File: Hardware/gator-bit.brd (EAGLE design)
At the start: 114.4 x 70.4 mm, 95 parts, among them J1 GATOR, J10 GATOR, J11 GATOR, J12 GATOR, J13 GATOR, J14 GATOR, J15 GATOR, J16 GATOR, J17 GATOR, J18 GATOR, J2 GATOR, J3 GATOR, J4 GATOR, J6 GATOR, J7 GATOR, J8 GATOR, J9 GATOR, U1 TPS63070, U2 micro:bit, U3 TXB0104, U4 ADJ REG 1.5A

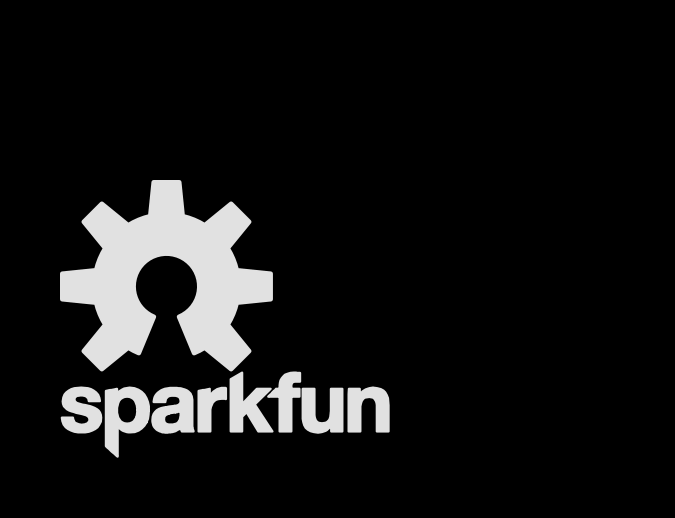
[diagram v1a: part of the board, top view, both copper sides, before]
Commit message: Updating per QC Review
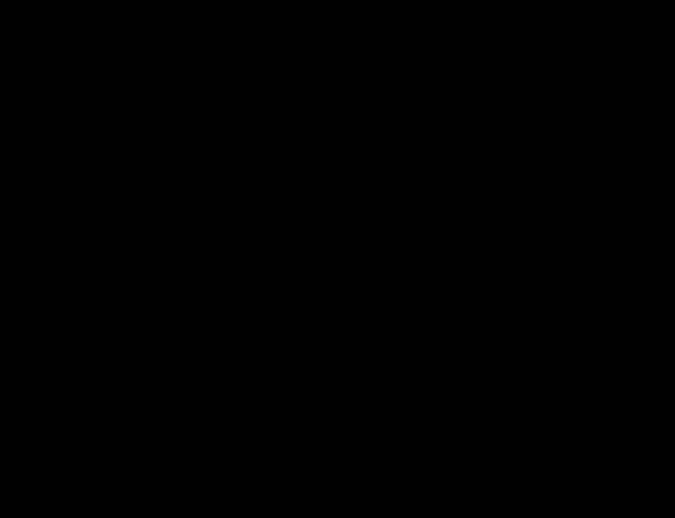
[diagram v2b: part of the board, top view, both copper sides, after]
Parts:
- removed LOGO1: OSHW-LOGOL, SparkFun-Aesthetics:OSHW-LOGO-L
- removed LOGO2: SFE_LOGO_NAME.1_INCH, SparkFun-Aesthetics:SFE_LOGO_NAME_.1
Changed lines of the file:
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@@
 <?xml version="1.0" encoding="utf-8"?>
 <!DOCTYPE eagle SYSTEM "eagle.dtd">
-<eagle version="7.7.0">
+<eagle version="8.5.1">
 <drawing>
 <settings>
 <setting alwaysvectorfont="no"/>
+<setting keepoldvectorfont="yes"/>
 <setting verticaltext="up"/>
 </settings>
@@
 <layers>
 <layer number="1" name="Top" color="4" fill="1" visible="yes" active="yes"/>
-<layer number="2" name="Route2" color="1" fill="3" visible="no" active="yes"/>
-<layer number="15" name="Route15" color="4" fill="6" visible="no" active="yes"/>
+<layer number="2" name="Route2" color="1" fill="3" visible="yes" active="yes"/>
+<layer number="15" name="Route15" color="4" fill="6" visible="yes" active="yes"/>
 <layer number="16" name="Bottom" color="1" fill="1" visible="yes" active="yes"/>
 <layer number="17" name="Pads" color="2" fill="1" visible="yes" active="yes"/>
@@
 <layer number="19" name="Unrouted" color="6" fill="1" visible="yes" active="yes"/>
 <layer number="20" name="Dimension" color="15" fill="1" visible="yes" active="yes"/>
-<layer number="21" name="tPlace" color="16" fill="1" visible="no" active="yes"/>
-<layer number="22" name="bPlace" color="14" fill="1" visible="no" active="yes"/>
+<layer number="21" name="tPlace" color="16" fill="1" visible="yes" active="yes"/>
+<layer number="22" name="bPlace" color="14" fill="1" visible="yes" active="yes"/>
 <layer number="23" name="tOrigins" color="15" fill="1" visible="yes" active="yes"/>
 <layer number="24" name="bOrigins" color="15" fill="1" visible="yes" active="yes"/>
-<layer number="25" name="tNames" color="7" fill="1" visible="no" active="yes"/>
-<layer number="26" name="bNames" color="7" fill="1" visible="no" active="yes"/>
-<layer number="27" name="tValues" color="7" fill="1" visible="no" active="yes"/>
-<layer number="28" name="bValues" color="7" fill="1" visible="no" active="yes"/>
+<layer number="25" name="tNames" color="7" fill="1" visible="yes" active="yes"/>
+<layer number="26" name="bNames" color="7" fill="1" visible="yes" active="yes"/>
+<layer number="27" name="tValues" color="7" fill="1" visible="yes" active="yes"/>
+<layer number="28" name="bValues" color="7" fill="1" visible="yes" active="yes"/>
 <layer number="29" name="tStop" color="7" fill="3" visible="yes" active="yes"/>
 <layer number="30" name="bStop" color="7" fill="6" visible="yes" active="yes"/>
@@
 <layer number="41" name="tRestrict" color="4" fill="10" visible="yes" active="yes"/>
 <layer number="42" name="bRestrict" color="1" fill="10" visible="yes" active="yes"/>
-<layer number="43" name="vRestrict" color="2" fill="10" visible="no" active="yes"/>
-<layer number="44" name="Drills" color="7" fill="1" visible="no" active="yes"/>
-<layer number="45" name="Holes" color="7" fill="1" visible="no" active="yes"/>
-<layer number="46" name="Milling" color="3" fill="1" visible="no" active="yes"/>
-<layer number="47" name="Measures" color="7" fill="1" visible="no" active="yes"/>
-<layer number="51" name="tDocu" color="6" fill="1" visible="no" active="yes"/>
-<layer number="52" name="bDocu" color="7" fill="1" visible="no" active="yes"/>
+<layer number="43" name="vRestrict" color="2" fill="10" visible="yes" active="yes"/>
+<layer number="44" name="Drills" color="7" fill="1" visible="yes" active="yes"/>
+<layer number="45" name="Holes" color="7" fill="1" visible="yes" active="yes"/>
+<layer number="46" name="Milling" color="3" fill="1" visible="yes" active="yes"/>
+<layer number="47" name="Measures" color="7" fill="1" visible="yes" active="yes"/>
+<layer number="51" name="tDocu" color="6" fill="1" visible="yes" active="yes"/>
+<layer number="52" name="bDocu" color="7" fill="1" visible="yes" active="yes"/>
 <layer number="3" name="Route3" color="4" fill="3" visible="no" active="no"/>
 <layer number="4" name="Route4" color="1" fill="4" visible="no" active="no"/>
@@
 <layer number="230" name="230bmp" color="7" fill="1" visible="no" active="no"/>
 <layer number="231" name="231bmp" color="7" fill="1" visible="no" active="no"/>
-<layer number="232" name="Eagle3D_PG2" color="7" fill="1" visible="no" active="yes"/>
-<layer number="233" name="Eagle3D_PG3" color="7" fill="1" visible="no" active="yes"/>
+<layer number="232" name="Eagle3D_PG2" color="7" fill="1" visible="yes" active="yes"/>
+<layer number="233" name="Eagle3D_PG3" color="7" fill="1" visible="yes" active="yes"/>
 <layer number="248" name="Housing" color="7" fill="1" visible="no" active="no"/>
 <layer number="249" name="Edge" color="7" fill="1" visible="no" active="no"/>
@@
 <param name="dpMaxLengthDifference" value="10mm"/>
 <param name="dpGapFactor" value="2.5"/>
-<param name="checkGrid" value="0"/>
 <param name="checkAngle" value="1"/>
 <param name="checkFont" value="1"/>
 <param name="checkRestrict" value="1"/>
+<param name="checkStop" value="0"/>
+<param name="checkValues" value="0"/>
 <param name="useDiameter" value="13"/>
 <param name="maxErrors" value="50"/>
@@
 <element name="FD3" library="SparkFun-Aesthetics" package="FIDUCIAL-1X2" value="FIDUCIAL1X2" x="109.22" y="4.2037"/>
 <element name="U4" library="SparkFun-IC-Power" package="SOT223" value="ADJ REG 1.5A" x="90.4875" y="60.0075" rot="R180">
+<attribute name="PROD_ID" value="VREG-12029" x="90.4875" y="60.0075" size="1.778" layer="27" rot="R180" display="off"/>
 <attribute name="VALUE" value="ADJ REG 1.5A" x="90.4875" y="60.0075" size="1.778" layer="27" rot="R180" display="off"/>
-<attribute name="PROD_ID" value="VREG-12029" x="90.4875" y="60.0075" size="1.778" layer="27" rot="R180" display="off"/>
 </element>
 <element name="R5" library="SparkFun-Resistors" package="0603" value="390k" x="96.3168" y="62.8396" rot="R270">
@@
 </element>
 <element name="S2" library="SparkFun-Switches" package="SWITCH_DPDT_SMD_AYZ0202" value="" x="96.1263" y="5.0038" rot="R270">
+<attribute name="PROD_ID" value="SWCH-08179" x="121.68505" y="23.26005" size="1.778" layer="27" rot="R270" display="off"/>
 <attribute name="SF_ID" value="COM-00597" x="121.68505" y="23.26005" size="1.778" layer="27" rot="R270" display="off"/>
-<attribute name="PROD_ID" value="SWCH-08179" x="121.68505" y="23.26005" size="1.778" layer="27" rot="R270" display="off"/>
 </element>
 <element name="D6" library="SparkFun-DiscreteSemi" package="SOD-323" value="1A/23V/620mV" x="103.66375" y="16.51">
@@
 <attribute name="PROD_ID" value="RES-08585" x="81.7372" y="40.5892" size="1.778" layer="27" display="off"/>
 </element>
-<element name="LOGO1" library="SparkFun-Aesthetics" package="OSHW-LOGO-L" value="OSHW-LOGOL" x="-17.145" y="-81.2546"/>
-<element name="LOGO2" library="SparkFun-Aesthetics" package="SFE_LOGO_NAME_.1" value="SFE_LOGO_NAME.1_INCH" x="-21.1328" y="-87.4268"/>
 </elements>
 <signals>

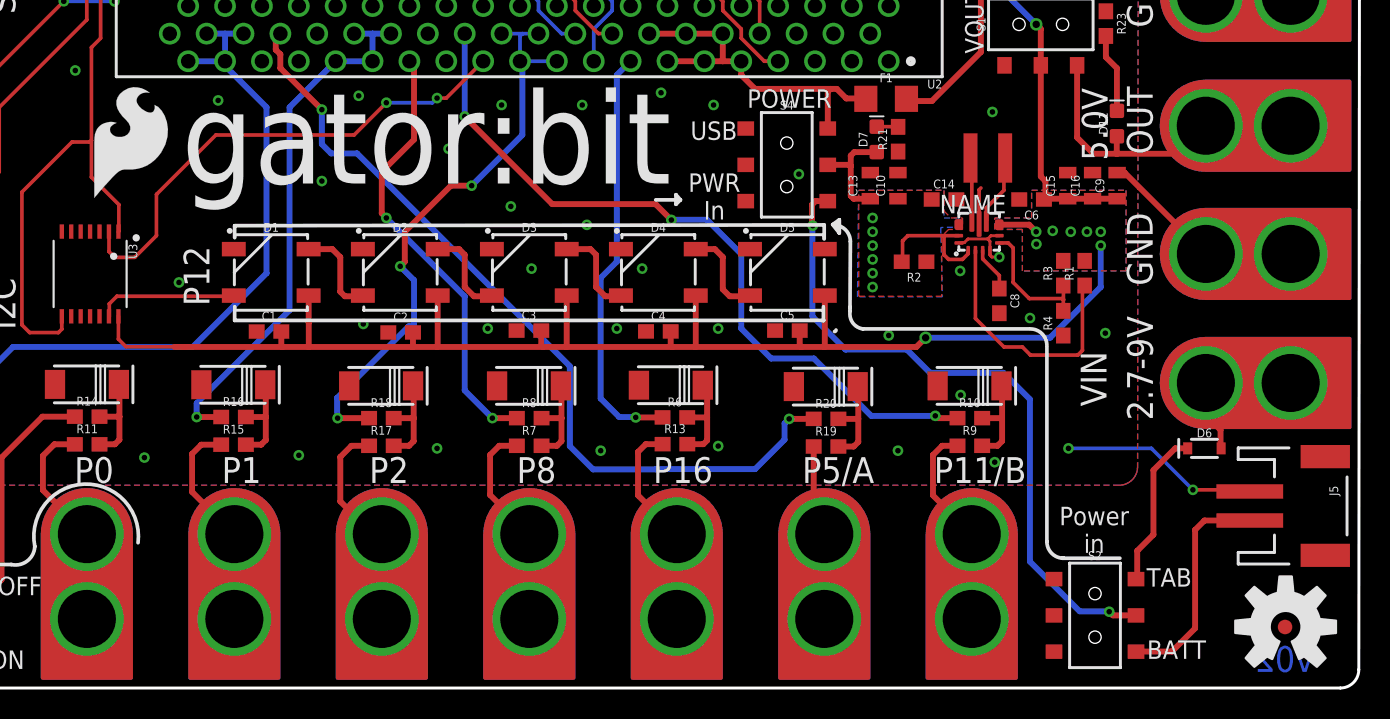
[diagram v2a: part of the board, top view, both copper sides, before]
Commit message: Updating TXB package
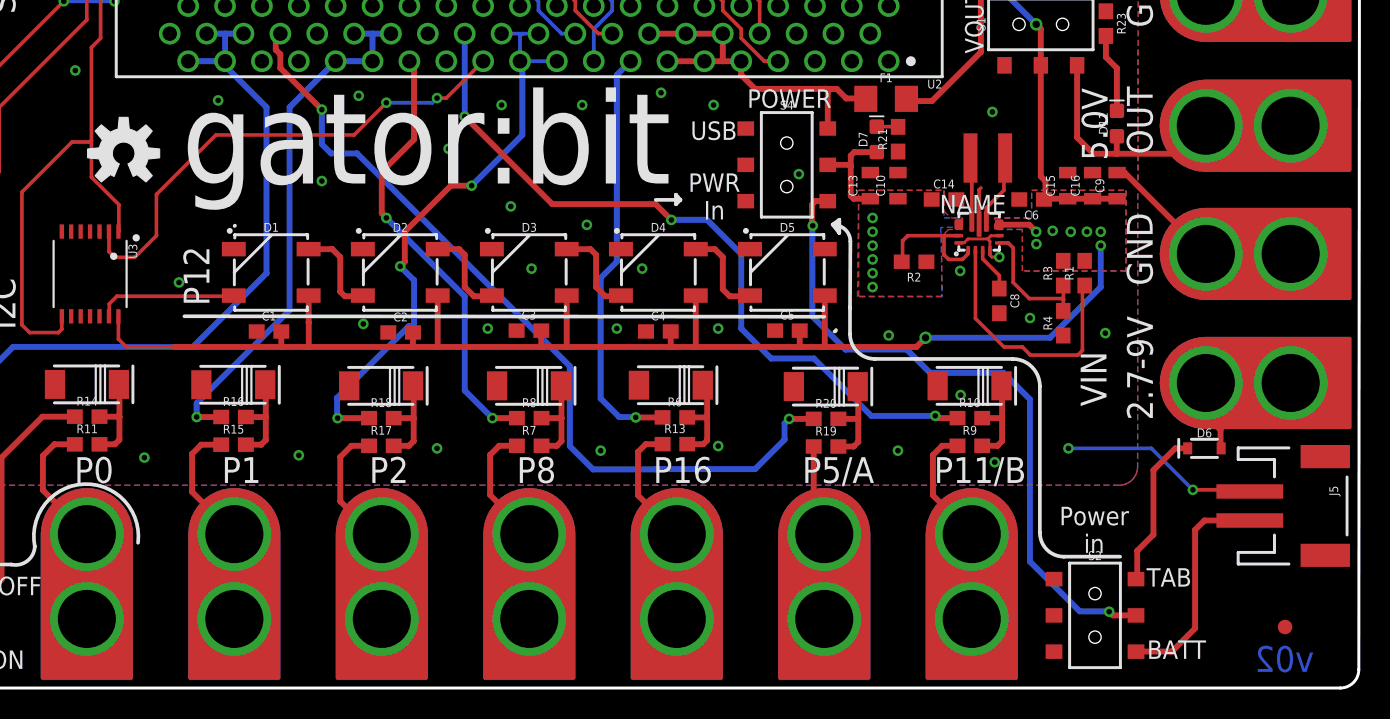
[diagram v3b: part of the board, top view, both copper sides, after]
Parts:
- removed LOGO4: SFE_LOGO_NAME_FLAME.3_INCH, SparkFun-Aesthetics:SFE_LOGO_NAME_FLAME_.3
- removed LOGO5: SFE_LOGO_FLAME.3_INCH, SparkFun-Aesthetics:SFE_LOGO_FLAME_.3
- removed LOGO6: OSHW-LOGOL, SparkFun-Aesthetics:OSHW-LOGO-L
- added LOGO1: SFE_LOGO_NAME_FLAME.3_INCH, SparkFun-Aesthetics:SFE_LOGO_NAME_FLAME_.3
- added LOGO2: OSHW-LOGOM, SparkFun-Aesthetics:OSHW-LOGO-M
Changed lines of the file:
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@@
 <?xml version="1.0" encoding="utf-8"?>
 <!DOCTYPE eagle SYSTEM "eagle.dtd">
-<eagle version="8.5.1">
+<eagle version="7.7.0">
 <drawing>
 <settings>
 <setting alwaysvectorfont="no"/>
-<setting keepoldvectorfont="yes"/>
 <setting verticaltext="up"/>
 </settings>
-<grid distance="0.001" unitdist="inch" unit="inch" style="lines" multiple="1" display="yes" altdistance="0.001" altunitdist="mil" altunit="inch"/>
+<grid distance="0.00125" unitdist="inch" unit="inch" style="lines" multiple="1" display="yes" altdistance="0.001" altunitdist="mil" altunit="inch"/>
 <layers>
 <layer number="1" name="Top" color="4" fill="1" visible="yes" active="yes"/>
@@
 <wire x1="78.1304" y1="31.9024" x2="79.2734" y2="30.7594" width="0.254" layer="21" curve="-90"/>
 <wire x1="79.2734" y1="30.7594" x2="79.248" y2="26.1874" width="0.254" layer="21"/>
-<wire x1="80.137" y1="24.7396" x2="91.5416" y2="24.7396" width="0.254" layer="21"/>
-<wire x1="92.8116" y1="23.4696" x2="92.8116" y2="10.0838" width="0.254" layer="21"/>
 <text x="77.974925" y="41.241978125" size="1.27" layer="21" font="vector" ratio="15" rot="R180">POWER</text>
-<wire x1="80.137" y1="24.7396" x2="79.248" y2="25.908" width="0.254" layer="21" curve="-90"/>
-<wire x1="91.6686" y1="24.7396" x2="92.8116" y2="23.5966" width="0.254" layer="21" curve="-90"/>
-<wire x1="79.248" y1="26.2382" x2="79.248" y2="25.9842" width="0.254" layer="21"/>
-<wire x1="93.8784" y1="8.9408" x2="93.9546" y2="8.9408" width="0.254" layer="21"/>
-<wire x1="93.9546" y1="8.9408" x2="97.8408" y2="8.9408" width="0.254" layer="21"/>
-<wire x1="93.9546" y1="8.9408" x2="92.8116" y2="10.0838" width="0.254" layer="21" curve="-90"/>
 <wire x1="78.0542" y1="31.9278" x2="78.5114" y2="32.258" width="0.254" layer="21"/>
 <wire x1="78.5114" y1="32.258" x2="78.5114" y2="31.3436" width="0.254" layer="21"/>
@@
 <wire x1="21.463" y1="8.509" x2="23.0886" y2="9.7536" width="0.254" layer="21" curve="100.388816"/>
 <wire x1="23.0886" y1="9.7536" x2="30.2006" y2="10.0076" width="0.254" layer="21" curve="-198.130762"/>
-<wire x1="36.8554" y1="25.3238" x2="77.4446" y2="25.3238" width="0.254" layer="21"/>
-<wire x1="77.47" y1="31.9024" x2="36.8808" y2="31.8516" width="0.254" layer="21"/>
+<wire x1="33.39465" y1="25.60955" x2="77.47635" y2="25.5778" width="0.254" layer="21"/>
 <wire x1="78.1812" y1="24.5618" x2="78.2828" y2="24.6634" width="0.254" layer="21" curve="90"/>
-<wire x1="77.47" y1="30.9372" x2="77.47" y2="31.9024" width="0.254" layer="21"/>
-<wire x1="77.4192" y1="25.2984" x2="77.4192" y2="26.2636" width="0.254" layer="21"/>
-<wire x1="36.8554" y1="31.0388" x2="36.8554" y2="31.8262" width="0.254" layer="21"/>
 <wire x1="36.8554" y1="31.8262" x2="36.8808" y2="31.8516" width="0.254" layer="21" curve="-90"/>
-<wire x1="36.8554" y1="26.2636" x2="36.8554" y2="25.3238" width="0.254" layer="21"/>
 <wire x1="65.8622" y1="33.6296" x2="67.564" y2="33.6296" width="0.254" layer="21"/>
 <wire x1="67.564" y1="33.6296" x2="67.2592" y2="33.9852" width="0.254" layer="21"/>
 <wire x1="67.2592" y1="33.9852" x2="67.2592" y2="33.3248" width="0.254" layer="21"/>
 <wire x1="67.2592" y1="33.3248" x2="67.564" y2="33.6296" width="0.254" layer="21"/>
+<wire x1="79.248" y1="26.2382" x2="79.248" y2="24.384" width="0.254" layer="21"/>
+<wire x1="79.248" y1="24.384" x2="80.9625" y2="22.6695" width="0.254" layer="21" curve="90"/>
+<wire x1="80.9625" y1="22.6695" x2="90.45575" y2="22.6695" width="0.254" layer="21"/>
+<wire x1="90.45575" y1="22.6695" x2="92.329" y2="20.79625" width="0.254" layer="21" curve="-90"/>
+<wire x1="92.329" y1="20.79625" x2="92.329" y2="10.69975" width="0.254" layer="21"/>
+<wire x1="92.329" y1="10.69975" x2="93.98" y2="9.04875" width="0.254" layer="21" curve="90"/>
+<wire x1="93.98" y1="9.04875" x2="97.8535" y2="9.04875" width="0.254" layer="21"/>
 </plain>
 <attributes>
@@
 <param name="dpMaxLengthDifference" value="10mm"/>
 <param name="dpGapFactor" value="2.5"/>
+<param name="checkGrid" value="0"/>
 <param name="checkAngle" value="1"/>
 <param name="checkFont" value="1"/>
 <param name="checkRestrict" value="1"/>
-<param name="checkStop" value="0"/>
-<param name="checkValues" value="0"/>
 <param name="useDiameter" value="13"/>
 <param name="maxErrors" value="50"/>
@@
 <element name="FD3" library="SparkFun-Aesthetics" package="FIDUCIAL-1X2" value="FIDUCIAL1X2" x="109.22" y="4.2037"/>
 <element name="U4" library="SparkFun-IC-Power" package="SOT223" value="ADJ REG 1.5A" x="90.4875" y="60.0075" rot="R180">
+<attribute name="VALUE" value="ADJ REG 1.5A" x="90.4875" y="60.0075" size="1.778" layer="27" rot="R180" display="off"/>
 <attribute name="PROD_ID" value="VREG-12029" x="90.4875" y="60.0075" size="1.778" layer="27" rot="R180" display="off"/>
-<attribute name="VALUE" value="ADJ REG 1.5A" x="90.4875" y="60.0075" size="1.778" layer="27" rot="R180" display="off"/>
 </element>
 <element name="R5" library="SparkFun-Resistors" package="0603" value="390k" x="96.3168" y="62.8396" rot="R270">
@@
 </element>
 <element name="S2" library="SparkFun-Switches" package="SWITCH_DPDT_SMD_AYZ0202" value="" x="96.1263" y="5.0038" rot="R270">
+<attribute name="SF_ID" value="COM-00597" x="121.68505" y="23.26005" size="1.778" layer="27" rot="R270" display="off"/>
 <attribute name="PROD_ID" value="SWCH-08179" x="121.68505" y="23.26005" size="1.778" layer="27" rot="R270" display="off"/>
-<attribute name="SF_ID" value="COM-00597" x="121.68505" y="23.26005" size="1.778" layer="27" rot="R270" display="off"/>
 </element>
 <element name="D6" library="SparkFun-DiscreteSemi" package="SOD-323" value="1A/23V/620mV" x="103.66375" y="16.51">
 <attribute name="PROD_ID" value="DIO-11623" x="83.82" y="42.06875" size="1.778" layer="27" display="off"/>
 </element>
-<element name="LOGO4" library="SparkFun-Aesthetics" package="SFE_LOGO_NAME_FLAME_.3" value="SFE_LOGO_NAME_FLAME.3_INCH" x="73.50125" y="15.39875" rot="MR0"/>
-<element name="LOGO5" library="SparkFun-Aesthetics" package="SFE_LOGO_FLAME_.3" value="SFE_LOGO_FLAME.3_INCH" x="26.68905" y="33.62325"/>
-<element name="LOGO6" library="SparkFun-Aesthetics" package="OSHW-LOGO-L" value="OSHW-LOGOL" x="109.2581" y="4.2164"/>
 <element name="C10" library="SparkFun-Capacitors" package="0805" value="10uF" x="82.55" y="34.6075" rot="R90">
 <attribute name="PROD_ID" value="CAP-11330" x="82.55" y="34.6075" size="1.778" layer="27" rot="R90" display="off"/>
@@
 </element>
 <element name="U3" library="SparkFun-IC-Comms" package="TSSOP14" value="TXB0104" x="26.8986" y="28.5242" rot="R180">
-<attribute name="PROD_ID" value="NA-XXXXX" x="26.8986" y="28.5242" size="1.778" layer="27" rot="R180" display="off"/>
+<attribute name="PROD_ID" value="IC-11329" x="26.8986" y="28.5242" size="1.778" layer="27" rot="R180" display="off"/>
 </element>
 <element name="D7" library="SparkFun-LED" package="LED-0603" value="RED" x="81.0895" y="37.7952" rot="R90">
@@
 <attribute name="PROD_ID" value="RES-08585" x="81.7372" y="40.5892" size="1.778" layer="27" display="off"/>
 </element>
+<element name="LOGO1" library="SparkFun-Aesthetics" package="SFE_LOGO_NAME_FLAME_.3" value="SFE_LOGO_NAME_FLAME.3_INCH" x="74.93" y="17.78" rot="MR0"/>
+<element name="LOGO2" library="SparkFun-Aesthetics" package="OSHW-LOGO-M" value="OSHW-LOGOM" x="29.21" y="36.83"/>
 </elements>
 <signals>
